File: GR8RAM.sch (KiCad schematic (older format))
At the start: 46 parts, among them J1 AppleIIBus, J2 JTAG, U1 EPM7128SL84, U2 512Kx8 Flash, U3 4Mx4 DRAM, U4 4Mx4 DRAM, U5 4Mx4 DRAM, U6 4Mx4 DRAM

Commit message: Removed AVR-JTAG-10 connector footprint
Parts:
- removed J2: JTAG, stdpads:IDC_SMD_2x05_P2.54mm_Vertical, symbol Connector:AVR-JTAG-10
- added J2: JTAG, stdpads:IDC_SMD_2x05_P2.54mm_Vertical, symbol Connector_Generic:Conn_02x05_Odd_Even
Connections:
- wire segments 229 -> 234
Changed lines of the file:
@@
 EESchema Schematic File Version 4
-LIBS:GR8RAM-cache
-EELAYER 29 0
+EELAYER 30 0
 EELAYER END
 $Descr USLetter 11000 8500
@@
 Text Label 5800 3600 2    50   ~ 0
 A9
-$Comp
-L power:+5V #PWR0118
-U 1 1 5DCF4586
-P 9450 5200
-F 0 "#PWR0118" H 9450 5050 50  0001 C CNN
-F 1 "+5V" H 9450 5350 50  0000 C CNN
-F 2 "" H 9450 5200 50  0001 C CNN
-F 3 "" H 9450 5200 50  0001 C CNN
-	1    9450 5200
-	1    0    0    -1
-$EndComp
 Wire Wire Line
 	3400 6400 3100 6400
@@
 	1    0    0    -1
 $EndComp
-Text Label 10050 5700 0    50   ~ 0
-TCK
-Text Label 10050 5800 0    50   ~ 0
-TMS
-Text Label 10050 5900 0    50   ~ 0
-TDO
-Text Label 10050 6000 0    50   ~ 0
-TDI
-$Comp
-L power:GND #PWR0122
-U 1 1 5DCF4205
-P 9550 6400
-F 0 "#PWR0122" H 9550 6150 50  0001 C CNN
-F 1 "GND" H 9550 6250 50  0000 C CNN
-F 2 "" H 9550 6400 50  0001 C CNN
-F 3 "" H 9550 6400 50  0001 C CNN
-	1    9550 6400
-	1    0    0    -1
-$EndComp
-$Comp
-L Connector:AVR-JTAG-10 J2
-U 1 1 5DCF2B5F
-P 9550 5800
-F 0 "J2" H 9550 5850 50  0000 C BNN
-F 1 "JTAG" H 9550 5800 50  0000 C CNN
-F 2 "stdpads:IDC_SMD_2x05_P2.54mm_Vertical" V 9400 5950 50  0001 C CNN
-F 3 " ~" H 8275 5250 50  0001 C CNN
-	1    9550 5800
-	1    0    0    -1
-$EndComp
-NoConn ~ 9550 5200
 $Comp
 L power:+5V #PWR0109
@@
 Text Label 2700 1950 2    50   ~ 0
 A12
-NoConn ~ 10050 5600
-NoConn ~ 10050 5500
 Text Label 9200 3450 2    50   ~ 0
 RA2
@@
 	10000 4250 10000 4350
 $Comp
-L power:GND #PWR?
+L power:GND #PWR0106
 U 1 1 5E6DB0A3
 P 10000 4350
-F 0 "#PWR?" H 10000 4100 50  0001 C CNN
+F 0 "#PWR0106" H 10000 4100 50  0001 C CNN
 F 1 "GND" H 10000 4200 50  0000 C CNN
 F 2 "" H 10000 4350 50  0001 C CNN
@@
 Wire Bus Line
 	6900 4800 8700 4800
+Text Label 9350 5300 2    50   ~ 0
+TCK
+Text Label 9350 5500 2    50   ~ 0
+TMS
+Text Label 9350 5400 2    50   ~ 0
+TDO
+Text Label 9350 5700 2    50   ~ 0
+TDI
+$Comp
+L power:+5V #PWR0129
+U 1 1 5E41A4F5
+P 10000 5500
+F 0 "#PWR0129" H 10000 5350 50  0001 C CNN
+F 1 "+5V" H 10000 5650 50  0000 C CNN
+F 2 "" H 10000 5500 50  0001 C CNN
+F 3 "" H 10000 5500 50  0001 C CNN
+	1    10000 5500
+	1    0    0    -1
+$EndComp
+Wire Wire Line
+	9950 5500 9850 5400
+$Comp
+L power:GND #PWR0130
+U 1 1 5E4376C1
+P 9850 5700
+F 0 "#PWR0130" H 9850 5450 50  0001 C CNN
+F 1 "GND" H 9850 5550 50  0000 C CNN
+F 2 "" H 9850 5700 50  0001 C CNN
+F 3 "" H 9850 5700 50  0001 C CNN
+	1    9850 5700
+	1    0    0    -1
+$EndComp
+Wire Wire Line
+	10000 5500 9950 5500
+NoConn ~ 9350 5600
+NoConn ~ 9850 5500
+NoConn ~ 9850 5600
+$Comp
+L Connector_Generic:Conn_02x05_Odd_Even J2
+U 1 1 5E4199B1
+P 9550 5500
+F 0 "J2" H 9600 5800 50  0000 C CNN
+F 1 "JTAG" H 9600 5200 50  0000 C CNN
+F 2 "stdpads:IDC_SMD_2x05_P2.54mm_Vertical" H 9550 5500 50  0001 C CNN
+F 3 "~" H 9550 5500 50  0001 C CNN
+	1    9550 5500
+	1    0    0    -1
+$EndComp
+Wire Wire Line
+	10100 5300 10100 5700
+Wire Wire Line
+	10100 5700 9850 5700
+Wire Wire Line
+	10100 5300 9850 5300
+Connection ~ 9850 5700
 Wire Bus Line
 	2400 1150 2400 2150
@@
 	2400 4650 2400 5850
 Wire Bus Line
-	8700 2000 8700 4800
-Wire Bus Line
-	10300 2000 10300 4800
-Wire Bus Line
 	4500 3550 4500 4800
 Wire Bus Line
@@
 	4500 1150 4500 3250
 Wire Bus Line
+	10300 2000 10300 4800
+Wire Bus Line
+	8700 2000 8700 4800
+Wire Bus Line
 	6900 3000 6900 4800

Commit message: Board done?
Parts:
- removed C11, C3, C4: 2u2, stdpads:C_0805, symbol Device:C_Small
- removed C14, C15, C16: DNP, stdpads:CP_EIA-3528, symbol Device:CP_Small
- removed JP1: Mode, Connector_PinHeader_2.54mm:PinHeader_1x02_P2.54mm_Vertical_SMD_Pin1Left, symbol Device:Jumper_NO_Small
- removed U1: EPM7128SL84, stdpads:PLCC-84_SMDSocket, symbol GW_PLD:EPM7128SL84
- removed U2: 512Kx8 Flash, stdpads:PLCC-32_SMDSocket, symbol GW_RAM:Flash-512Kx8-PLCC-32
- removed U3, U4, U5, U6: 4Mx4 DRAM, stdpads:SOP-24-26-300mil, symbol GW_RAM:DRAM-4Mx4-SOP-24
- added C14, C15, C16, C17, C19, C20, C23, C24, C25, C26, C27, C28, C29, C30, C31, C32, C33, C34, C35: 2u2, stdpads:C_0603, symbol Device:C_Small
- added C36, C37: 10u, stdpads:C_0805, symbol Device:C_Small
- added C38: 22n, stdpads:R_0805, symbol Device:C_Small
- added D1, D3: SS14, stdpads:D_SMA, symbol Device:D_Schottky_Small_ALT
- added D2: SMBJ5.0A, stdpads:D_SMB, symbol Device:D_Zener_Small_ALT
- added F1: nSMD035-16V, stdpads:BelFuse_1206, symbol Device:Polyfuse_Small
- added FB1: GZ2012D601TF, stdpads:Murata_BLM21, symbol Device:Ferrite_Bead_Small
- added H6: (no value), stdpads:PasteHole_1.152mm_NPTH, symbol Mechanical:MountingHole_Pad
- added J3: DC in, stdpads:BOOMELE_DC-005_DC_5.5-2.0MM, symbol Connector:Barrel_Jack_Switch
- added J4: JTAG, Connector_IDC:IDC-Header_2x05_P2.54mm_Vertical, symbol Connector_Generic:Conn_02x05_Odd_Even
- added Q1: AO3401A, stdpads:SOT-23, symbol Transistor_FET:AO3401A
- added R10, R11, R12, R6, R7: 1k, stdpads:R_0805, symbol Device:R_Small
- added R13: 100, stdpads:R_0805, symbol Device:R_Small
- added R14: 0, stdpads:R_0805, symbol Device:R_Small
- added R8: 1M, stdpads:R_0805, symbol Device:R_Small
- added R9: 3k3, stdpads:R_0805, symbol Device:R_Small
- added RN1, RN2, RN3: 4x33, stdpads:R4_0402, symbol Device:R_Pack04
- added RN4: 4x10k, stdpads:R4_0402, symbol Device:R_Pack04
- added U1: EPM240T100C5N, stdpads:TQFP-100_14x14mm_P0.5mm, symbol GW_PLD:EPM240T100
- added U12, U14: 74AHCT125, stdpads:TSSOP-14_4.4x5mm_P0.65mm, symbol GW_Logic:74125
- added U13: 25M, stdpads:Crystal_SMD_3225-4Pin_3.2x2.5mm, symbol GW_Logic:Oscillator_4P
- added U16: 74LVC1G04GW, stdpads:SOT-353, symbol GW_Logic:741G04GW
- added U2: W9825, stdpads:TSOP-II-54_22.2x10.16mm_P0.8mm, symbol GW_RAM:SDRAM-16Mx16-TSOP2-54
- added U3: MX29LV640EB, stdpads:TSOP-I-48_18.4x12mm_P0.5mm, symbol GW_RAM:Flash-4Mx16-TSOP1-48
- added U4, U5, U6, U9: 74AHC245, stdpads:TSSOP-20_4.4x6.5mm_P0.65mm, symbol GW_Logic:74245
- added U7: LM393, stdpads:SOIC-8_3.9mm, symbol Comparator:LM393
- added U8: AP2125, stdpads:SOT-23, symbol GW_Power:AP2125
- C1, C10, C5, C6, C7, C8: value 2u2 -> 10u; LCSC Part (none) -> C15850
- C11: renamed from C9; value 2u2 -> 10u; LCSC Part (none) -> C15850
- C12, C13, C18, C21, C22: footprint stdpads:C_0805 -> stdpads:C_0603; LCSC Part (none) -> C23630
- C2: renamed from C20; value 2u2 -> 10u; LCSC Part (none) -> C15850
- C3: renamed from C17; value 2u2 -> 10u; LCSC Part (none) -> C15850
- C4: renamed from C19; value 2u2 -> 10u; LCSC Part (none) -> C15850
- C9: renamed from C2; footprint stdpads:C_0805 -> stdpads:C_0603; LCSC Part (none) -> C23630
- H2, H3, H4, H5: footprint stdpads:PasteHole_1.1mm_PTH -> stdpads:PasteHole_1.152mm_NPTH
- J2: footprint stdpads:IDC_SMD_2x05_P2.54mm_Vertical -> Connector:Tag-Connect_TC2050-IDC-FP_2x05_P1.27mm_Vertical
- R1, R2: value 100 -> DNP
- R3: value 100 -> 2k7; LCSC Part (none) -> C17530
- R4: value 15 -> 2k2; LCSC Part (none) -> C17520
- R5: value 22k -> 1M; LCSC Part (none) -> C17514
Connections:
- net labels added: +3V3, ACLK, Adir, A~OE~, DET, DMA~OE~, Ddir, Dr0, Dr1, Dr2, Dr3, Dr4, Dr5, Dr6, Dr7, D~OE~, INH~OE~, IRQ~OE~, NMI~OE~, RA11, RA12, RA13, RA14, RA15, RB0, RB1, RB10, RB11, RB2, RB3, RB4, RB5, RB6, RB7, RB8, RB9, RCLK, RDMAin, RDMAout, RINTin, RINTout, RPHI1, RR~W~in, RR~W~out, RW~OE~, R~DEVSEL~, R~IOSEL~, R~IOSTRB~, R~RES~, SA0, SA1, SA10, SA11, SA12, SA2, SA3, SA4, SA5, SA6, SA7, SA8, SA9, SBA0, SBA1, SCKE, SD0, SD1, SD2, SD3, SD4, SD5, SD6, SD7, SDQMH, SDQML, S~CAS~, S~CS~, S~RAS~, S~WE~, VBUS, Vin, ~DMA~, ~PreBOD~, ~RES~i
- net labels removed: 7Mr, C7Mout, DMA, PHI0r, PHI1out, PHI1r, Q3r, ~CAS~0, ~CAS~1, ~MODE~, ~RAS~
- wire segments 234 -> 304
- no-connect marks 4 -> 21
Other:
- note added: "~RES~ (+) input is 1.05V @ 4.2V\n~PreBOD~ (+) inpt is 1.0465V @ 4.5V\n 1.1628V @ 5.0V\n 1.2791V @ 5.5V"
- moved on the sheet: C11, C12, C2, C3, C4, C9, FID2, FID3, J1, J2

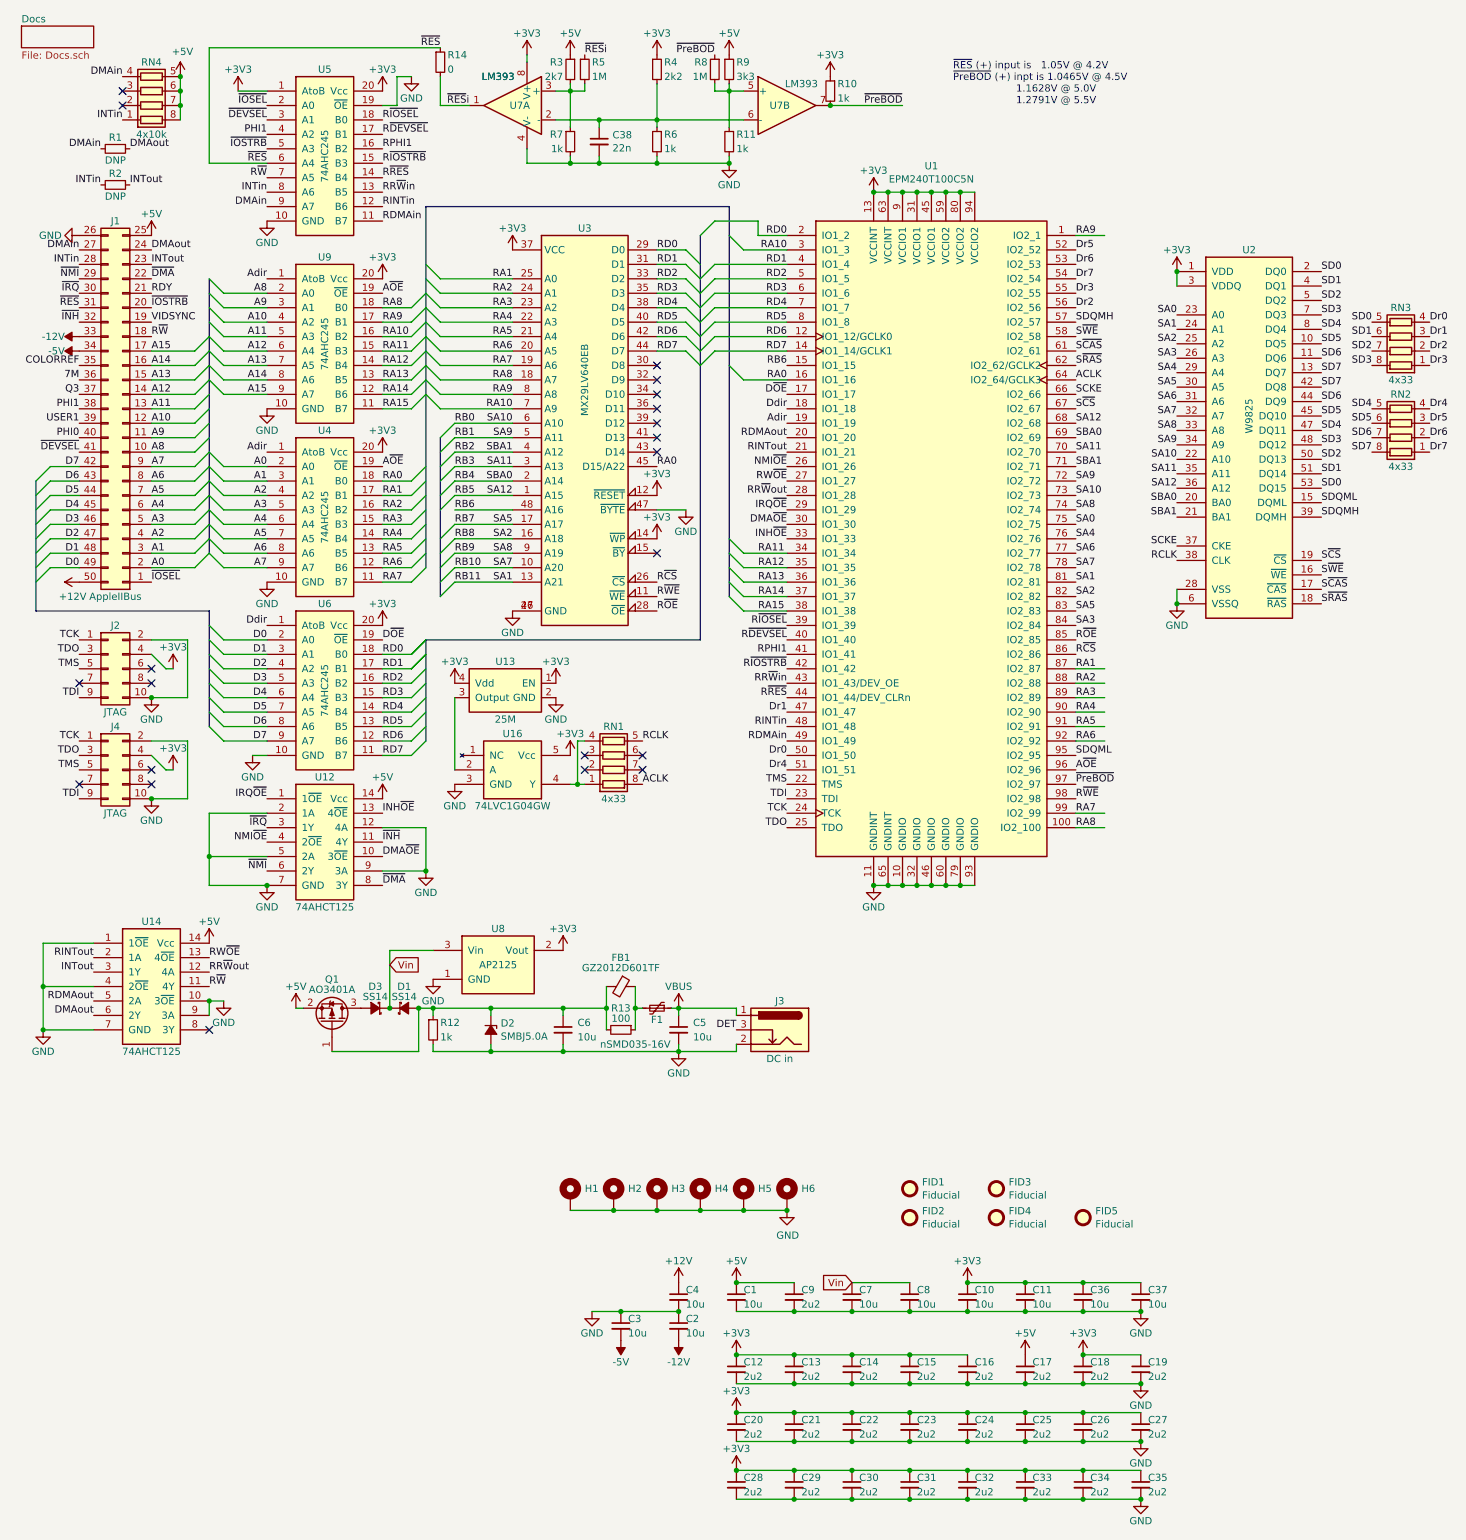
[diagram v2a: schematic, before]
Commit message: reset button detect
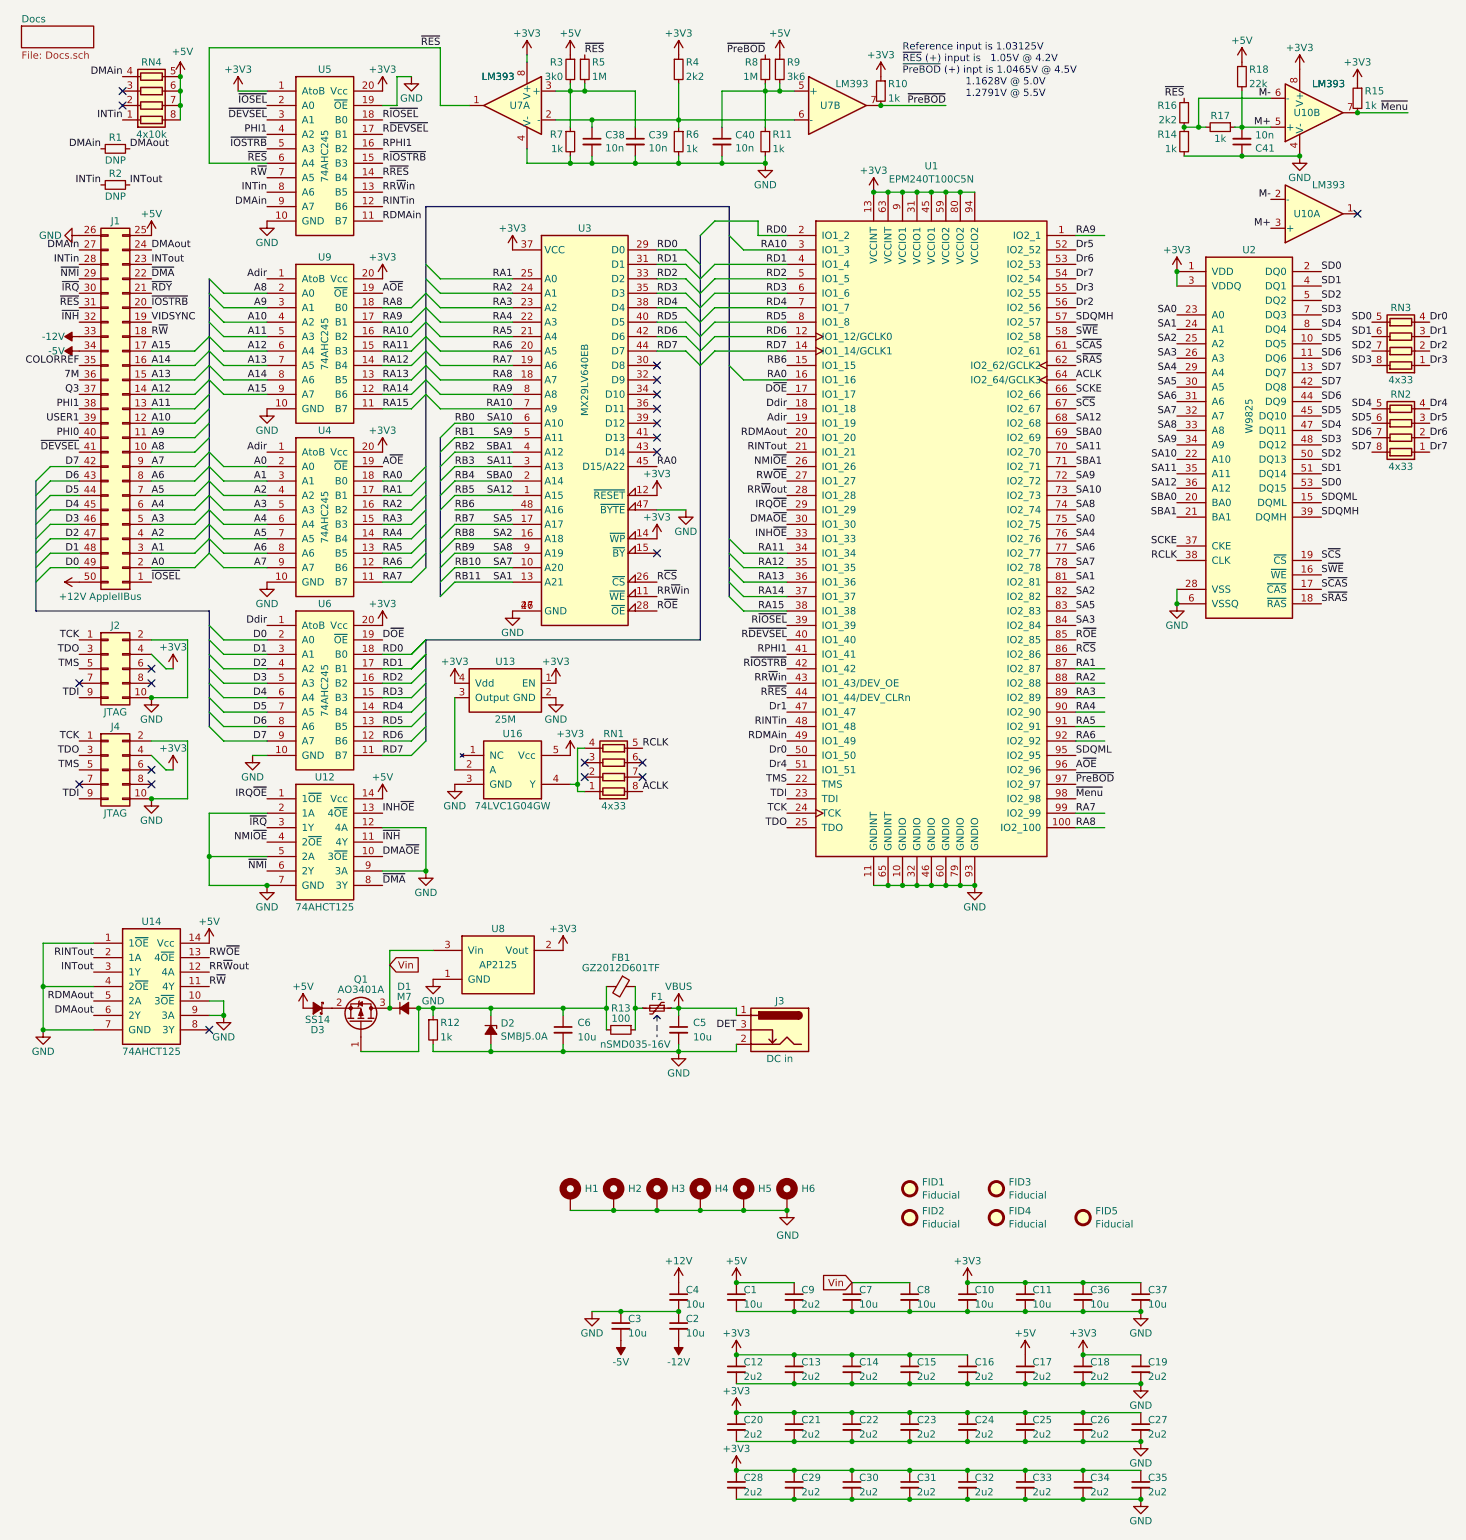
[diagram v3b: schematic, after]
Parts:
- removed D1: SS14, stdpads:D_SMA, symbol Device:D_Schottky_Small_ALT
- added C39, C40, C41: 10n, stdpads:C_0603, symbol Device:C_Small
- added D1: M7, stdpads:D_SMA, symbol Device:D_Small_ALT
- added R15, R17: 1k, stdpads:R_0603, symbol Device:R_Small
- added R16: 2k2, stdpads:R_0603, symbol Device:R_Small
- added R18: 22k, stdpads:R_0603, symbol Device:R_Small
- added U10: LM393, stdpads:SOIC-8_3.9mm, symbol Comparator:LM393
- C38: value 22n -> 10n; footprint stdpads:R_0805 -> stdpads:C_0603; LCSC Part C1729 -> C57112
- R10, R11, R6, R7: footprint stdpads:R_0805 -> stdpads:R_0603; LCSC Part C17513 -> C21190
- R14: value 0 -> 1k; footprint stdpads:R_0805 -> stdpads:R_0603; LCSC Part C17477 -> C21190
- R3: value 2k7 -> 3k0; footprint stdpads:R_0805 -> stdpads:R_0603; LCSC Part C17530 -> C4211
- R4: footprint stdpads:R_0805 -> stdpads:R_0603; LCSC Part C17520 -> C4190
- R5, R8: footprint stdpads:R_0805 -> stdpads:R_0603; LCSC Part C17514 -> C22935
- R9: value 3k3 -> 3k6; footprint stdpads:R_0805 -> stdpads:R_0603; LCSC Part C26010 -> C22980
- RN4: LCSC Part C25501 -> C25725
- U13: LCSC Part C61219 -> C32526
- U3: LCSC Part C30076 -> C34469
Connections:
- net +3V3: now also R15.1, U10.8 (V+)
- net +5V: now also D3.2 (A), R18.1; no longer Q1.2 (S)
- net GND: now also R14.2, C39.2, C40.2, C41.1, U10.4 (V-)
- net RR~W~in: now also U3.11 (~WE~)
- net Vin: now also Q1.3 (D), D1.1 (K); no longer D3.1 (K)
- net ~RES~: now also R5.1, U7.1, R16.1; no longer R14.1
- net at R3.2, R5.2, R7.1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: now also C39.1
- net at C6.1, D2.1 (K), FB1.2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: now also D1.2 (A)
- net at R11.1, R8.2, R9.2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: now also C40.1
- net RDY renamed ~RDY~
- net R~WE~ renamed ~Menu~
- net ~Menu~: now also R15.2, U10.7; no longer U3.11 (~WE~)
- removed net ~RES~i: R14.2, R5.1, U7.1
- new net: D3.1 (K), Q1.2 (S)
- new net M+: C41.2, R17.1, R18.2, U10.3 (+), U10.5 (+)
- new net M-: R14.1, R16.2, R17.2, U10.2 (-), U10.6 (-)
- no-connect marks 21 -> 22
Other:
- note added: "Reference input is 1.03125V\n~RES~ (+) input is 1.05V @ 4.2V\n~PreBOD~ (+) inpt is 1.0465V @ 4.5V\n 1.1628V @ 5.0V\n 1.2791V @ 5.5V"
- note removed: "~RES~ (+) input is 1.05V @ 4.2V\n~PreBOD~ (+) inpt is 1.0465V @ 4.5V\n 1.1628V @ 5.0V\n 1.2791V @ 5.5V"
- moved on the sheet: C38, D3, Q1, R10, R11, R4, R6, R8, R9, RN1, U7B
